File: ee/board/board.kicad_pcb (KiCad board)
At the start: 4 copper layers, 90 x 50 mm, 63 parts, among them J2 USB_A, J3 Micro_SD_Card_Det_Hirose_DM3AT, J4 Conn_01x08_Pin, J5 Conn_01x10_Pin, J6 Conn_Coaxial, SW1 SW_Push, U1 JW5211, U2 JW5211, U3 JW5211, U4 F1C100s, U5 SST26VF080A-104I/SN, U6 USBLC6-2SC6, U7 ATECC608A-SSHDA, Y1 Crystal_GND24

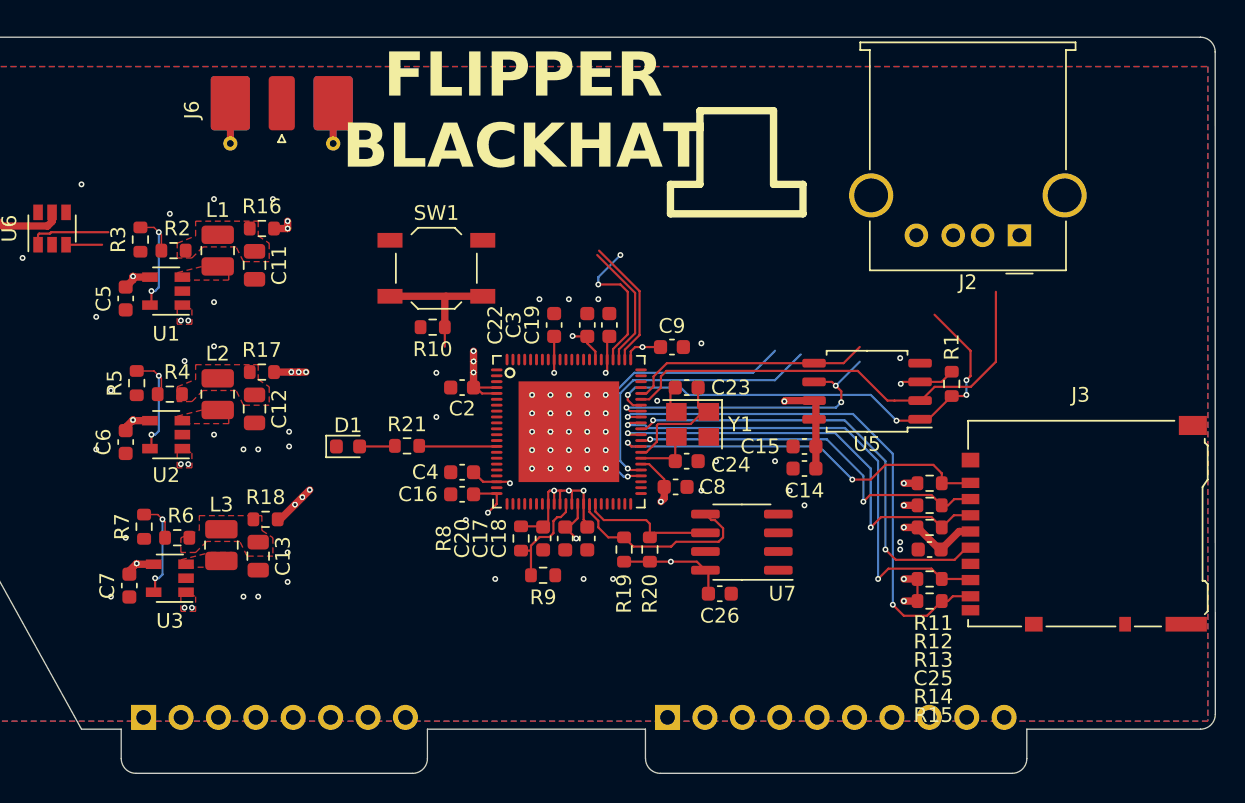
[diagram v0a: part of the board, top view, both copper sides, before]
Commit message: Dropped in the M.2 connectors.
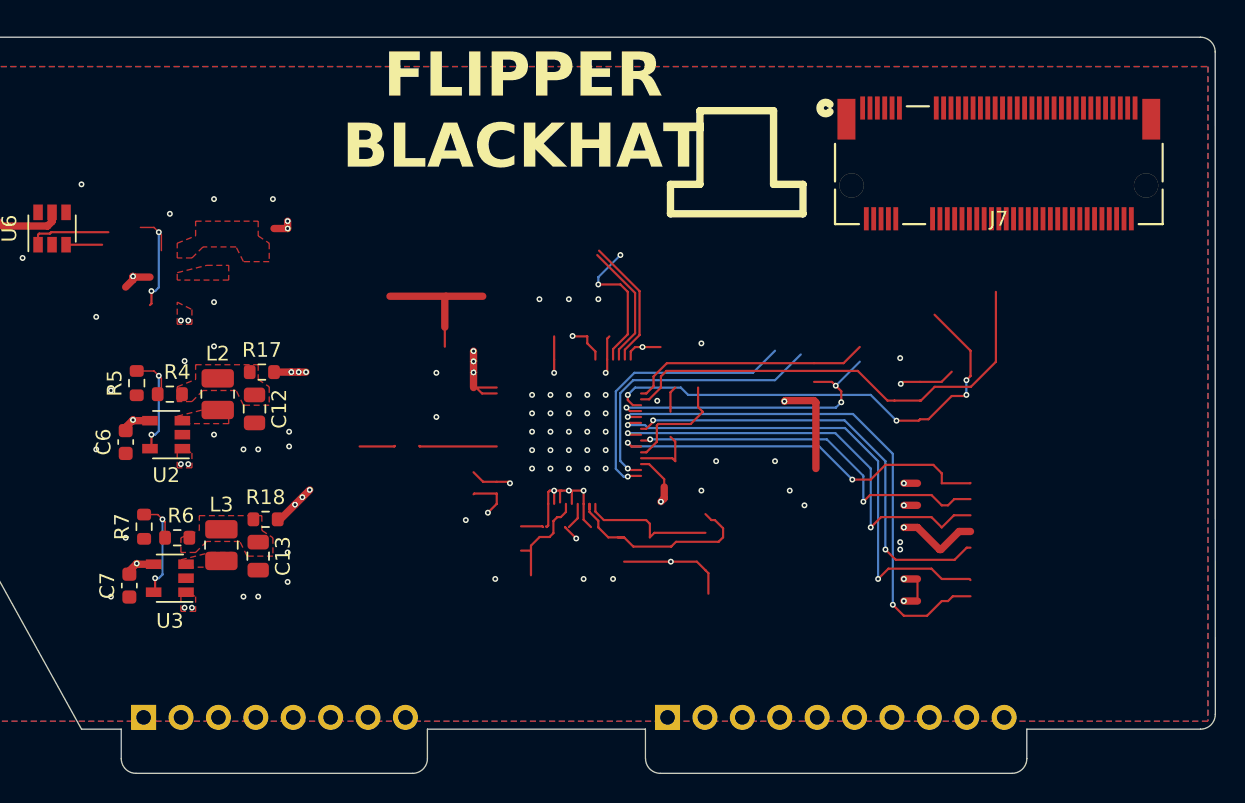
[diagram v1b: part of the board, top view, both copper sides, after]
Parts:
- removed C11: 22uF, Capacitor_SMD:C_0805_2012Metric
- removed C14, C15, C16, C2, C22, C25, C26, C3, C4, C8: 100nF, Capacitor_SMD:C_0603_1608Metric
- removed C17, C18, C19, C20, C5, C9: 2.2uF, Capacitor_SMD:C_0603_1608Metric
- removed C23, C24: 30pF, Capacitor_SMD:C_0603_1608Metric
- removed D1: LED, LED_SMD:LED_0603_1608Metric
- removed J2: USB_A, Connector_USB:USB_A_Molex_67643_Horizontal
- removed J3: Micro_SD_Card_Det_Hirose_DM3AT, Connector_Card:microSD_HC_Hirose_DM3AT-SF-PEJM5
- removed J6: Conn_Coaxial, Connector_Coaxial:SMA_Molex_73251-2120_EdgeMount_Horizontal
- removed L1: 1.5uH, Inductor_SMD:L_1008_2520Metric
- removed R1, R10: 10k, Resistor_SMD:R_0603_1608Metric
- removed R11, R12, R13, R14, R15: 47k, Resistor_SMD:R_0603_1608Metric
- removed R16: 0R, Resistor_SMD:R_0603_1608Metric
- removed R19, R20, R21: 4.7k, Resistor_SMD:R_0603_1608Metric
- removed R2: 49.9k, Resistor_SMD:R_0603_1608Metric
- removed R3: 11k, Resistor_SMD:R_0603_1608Metric
- removed R8, R9: 2.2k, Resistor_SMD:R_0603_1608Metric
- removed SW1: SW_Push, Button_Switch_SMD:SW_SPST_TL3342
- removed U1: JW5211, Package_TO_SOT_SMD:SOT-23-5
- removed U4: F1C100s, 3340:QFN-88_EP_10x10_Pitch0.4mm
- removed U5: SST26VF080A-104I/SN, Package_SO:SOIC-8_5.275x5.275mm_P1.27mm
- removed U7: ATECC608A-SSHDA, Package_SO:SOIC-8_3.9x4.9mm_P1.27mm
- removed Y1: Crystal_GND24, Crystal:Crystal_SMD_Abracon_ABM8G-4Pin_3.2x2.5mm
- added J7: Conn_01x20_Pin, 2199119-5:CONN75_2199119-5_TEC, F.Cu at (175.3, 98.7)
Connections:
- U6 pad 4: Net-(J2-D+) -> unconnected-(U6-I/O2-Pad4)
- U6 pad 6: Net-(J2-D-) -> unconnected-(U6-I/O1-Pad6)
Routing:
- net (no net): track 0.00 -> 402.4 mm, vias 0 -> 25
- net /SDC0_D1: track 36.5 -> 0.00 mm, vias 2 -> 0
- net /SDC0_D0: track 33.9 -> 0.00 mm, vias 2 -> 0
- net /SPI_CS: track 32.7 -> 0.00 mm, vias 4 -> 0
- net /SPI_MISO: track 32.0 -> 0.00 mm
- net /SDC0_CLK: track 30.5 -> 0.00 mm, vias 2 -> 0
- net /SDC0_CMD: track 30.1 -> 0.00 mm, vias 2 -> 0
- net /SDC0_D2: track 26.7 -> 0.00 mm, vias 2 -> 0
- net /SDC0_D3: track 25.8 -> 0.00 mm, vias 2 -> 0
- net /SPI_CK: track 21.0 -> 0.00 mm, vias 3 -> 0
- net /UART_RX: track 19.6 -> 0.00 mm, vias 1 -> 0
- net /!RST: track 19.6 -> 0.00 mm, vias 2 -> 0
- net /UART_TX: track 19.2 -> 0.00 mm, vias 1 -> 0
- net /SPI_MOSI: track 16.5 -> 0.00 mm
- net /TWI0_SDA: track 14.1 -> 0.00 mm
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- added copper zone on F.Cu, net (none)
- removed copper zone on F.Cu, net Net-(C11-Pad1)
- removed copper zone on F.Cu, net Net-(L1-Pad1)

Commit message: Added in module
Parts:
- removed C12, C13: 22uF, Capacitor_SMD:C_0805_2012Metric
- removed C6, C7: 2.2uF, Capacitor_SMD:C_0603_1608Metric
- removed F1: 330 mA, Fuse:Fuse_0603_1608Metric
- removed J7: Conn_01x20_Pin, 2199119-5:CONN75_2199119-5_TEC
- removed L2, L3: 1.5uH, Inductor_SMD:L_1008_2520Metric
- removed R17, R18: 0R, Resistor_SMD:R_0603_1608Metric
- removed R4: 36k, Resistor_SMD:R_0603_1608Metric
- removed R5: 11k, Resistor_SMD:R_0603_1608Metric
- removed R6: 8.2k, Resistor_SMD:R_0603_1608Metric
- removed R7: 10k, Resistor_SMD:R_0603_1608Metric
- removed U2, U3: JW5211, Package_TO_SOT_SMD:SOT-23-5
- added J1: Lichee_RV_J3, 2199119-5:CONN75_2199119-5_TEC, F.Cu at (164.0, 125.0)
- added J2: Lichee_RV_J4, 2199119-5:CONN75_2199119-5_TEC, F.Cu at (139.8, 125.0)
- added J3: USB_A, Connector_USB:USB_A_Receptacle_GCT_USB1046, F.Cu at (109.2, 99.1)
- added R1: 22R, Resistor_SMD:R_0603_1608Metric, F.Cu at (124.9, 104.2)
- added R2: 22R, Resistor_SMD:R_0603_1608Metric, F.Cu at (124.9, 106.7)
- moved U6 9.93 mm to (110.2, 112.9), turned to -90 degrees
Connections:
- J5 pad 5: /TX -> /UART_TXD
- J5 pad 6: /RX -> /UART_RXD
- U6 pad 1: /USB_N -> Net-(R2-Pad1)
- U6 pad 3: /USB_P -> Net-(R1-Pad1)
- U6 pad 4: unconnected-(U6-I/O2-Pad4) -> Net-(J3-D+)
- U6 pad 5: VBUS -> +5V
- U6 pad 6: unconnected-(U6-I/O1-Pad6) -> Net-(J3-D-)
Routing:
- net (no net): track 402.4 -> 0.00 mm, vias 25 -> 1
- net +3V3: track 47.9 -> 0.00 mm, vias 17 -> 0
- net +2V5: track 16.4 -> 0.00 mm, vias 9 -> 0
- net /USB_N: track 14.5 -> 0.00 mm
- net +1V1: track 11.6 -> 0.00 mm, vias 6 -> 0
- net /USB_P: track 11.1 -> 0.00 mm
- net VBUS: track 9.66 -> 0.00 mm
- net /2v5_FB: track 8.05 -> 0.00 mm, vias 2 -> 0
- net /1v1_FB: track 8.05 -> 0.00 mm, vias 2 -> 0
- net +5V: track 6.60 -> 0.00 mm, vias 19 -> 0
- net Net-(U2-EN): track 4.21 -> 0.00 mm, vias 2 -> 0
- net GND: track 1.78 -> 0.00 mm, vias 64 -> 0
- removed copper zone on F.Cu, net (none)
- removed copper zone on In1.Cu, net +1V1
- removed copper zone on In1.Cu, net +2V5
- removed copper zone on In1.Cu, net +3V3
- removed copper zone on F.Cu, net +5V
- removed copper zone on In1.Cu, net +5V
- removed copper zone on F.Cu, net Net-(C12-Pad1)
- removed copper zone on F.Cu, net Net-(C13-Pad1)
- removed copper zone on F.Cu, net Net-(U2-SW)
- removed copper zone on F.Cu, net Net-(U3-SW)

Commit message: Schematic mostly finished.
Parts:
- added C1: 10uF, Capacitor_SMD:C_0603_1608Metric, F.Cu at (139.7, 105.7)
- added C10: 100nF, Capacitor_SMD:C_0603_1608Metric, F.Cu at (217.9, 96.7)
- added C11: 100nF, Capacitor_SMD:C_0603_1608Metric, F.Cu at (217.9, 99.2)
- added C12: 100nF, Capacitor_SMD:C_0603_1608Metric, F.Cu at (217.9, 101.8)
- added C13: 22nF, Capacitor_SMD:C_0603_1608Metric, F.Cu at (176.3, 117.5)
- added C14: 18pF, Capacitor_SMD:C_0603_1608Metric, F.Cu at (221.9, 91.7)
- added C15: 18pF, Capacitor_SMD:C_0603_1608Metric, F.Cu at (221.9, 94.2)
- added C18: 22nF, Capacitor_SMD:C_0603_1608Metric, F.Cu at (221.9, 96.7)
- added C2: 10uF, Capacitor_SMD:C_0603_1608Metric, F.Cu at (139.7, 108.2)
- added C3: 10uF, Capacitor_SMD:C_0603_1608Metric, F.Cu at (139.7, 110.7)
- added C4: 10uF, Capacitor_SMD:C_0603_1608Metric, F.Cu at (139.7, 113.2)
- added C5: NC, Capacitor_SMD:C_0603_1608Metric, F.Cu at (139.7, 115.7)
- added C6: NC, Capacitor_SMD:C_0603_1608Metric, F.Cu at (151.4, 117.8)
- added C7: NC, Capacitor_SMD:C_0603_1608Metric, F.Cu at (151.4, 120.4)
- added C8: 100nF, Capacitor_SMD:C_0603_1608Metric, F.Cu at (217.9, 91.7)
- added C9: 1nF, Capacitor_SMD:C_0603_1608Metric, F.Cu at (217.9, 94.2)
- added H1: M2.5 Spacer, KiLib:9774025151R, F.Cu at (139.7, 105.7)
- added J6: Conn_Coaxial, Connector_Coaxial:SMA_Amphenol_901-143_Horizontal, F.Cu at (143.9, 96.5)
- added J8: HR911105A, KiLib:HR911105a, F.Cu at (171.0, 103.2)
- added JP1: SolderJumper_2_Bridged, Jumper:SolderJumper-2_P1.3mm_Bridged2Bar_RoundedPad1.0x1.5mm, F.Cu at (154.3, 104.2)
- added JP2: SolderJumper_2_Bridged, Jumper:SolderJumper-2_P1.3mm_Bridged2Bar_RoundedPad1.0x1.5mm, F.Cu at (155.6, 118.4)
- added JP3: SolderJumper_2_Bridged, Jumper:SolderJumper-2_P1.3mm_Bridged2Bar_RoundedPad1.0x1.5mm, F.Cu at (155.6, 121.9)
- added R13: 10k, Resistor_SMD:R_0603_1608Metric, F.Cu at (194.1, 74.8)
- added R14: 0R, Resistor_SMD:R_0603_1608Metric, F.Cu at (194.1, 77.9)
- added R15: 100K, Resistor_SMD:R_0603_1608Metric, F.Cu at (191.3, 64.7)
- added R16: 1k, Resistor_SMD:R_0603_1608Metric, F.Cu at (184.3, 64.7)
- added R17: 1k, Resistor_SMD:R_0603_1608Metric, F.Cu at (181.1, 64.7)
- added R18: 10K, Resistor_SMD:R_0603_1608Metric, F.Cu at (151.4, 112.2)
- added R19: 100R, Resistor_SMD:R_0603_1608Metric, F.Cu at (151.4, 122.9)
- added R21: 5.1k, Resistor_SMD:R_0603_1608Metric, F.Cu at (221.9, 99.2)
- added R3: 0R, Resistor_SMD:R_0603_1608Metric, F.Cu at (159.2, 96.5)
- added R30: 5.1k, Resistor_SMD:R_0603_1608Metric, F.Cu at (225.9, 104.3)
- added R31: 470R, Resistor_SMD:R_0603_1608Metric, F.Cu at (229.9, 91.7)
- added R32: 5.1k, Resistor_SMD:R_0603_1608Metric, F.Cu at (229.9, 94.2)
- added R33: 5.1k, Resistor_SMD:R_0603_1608Metric, F.Cu at (229.9, 96.7)
- added R34: 470R, Resistor_SMD:R_0603_1608Metric, F.Cu at (229.9, 99.2)
- added R4: 100K, Resistor_SMD:R_0603_1608Metric, F.Cu at (154.8, 96.5)
- added RN1: 10k, Resistor_SMD:R_Array_Convex_4x0402, F.Cu at (186.1, 80.6)
- added RN2: 10k, Resistor_SMD:R_Array_Convex_4x0402, F.Cu at (182.6, 80.6)
- added RN3: 10k, Resistor_SMD:R_Array_Convex_4x0402, F.Cu at (171.6, 124.0)
- added RN4: 10k, Resistor_SMD:R_Array_Convex_4x0402, F.Cu at (166.1, 118.2)
- added RN5: 22R, Resistor_SMD:R_Array_Convex_4x0402, F.Cu at (202.0, 110.3)
- added RN6: 22R, Resistor_SMD:R_Array_Convex_4x0402, F.Cu at (205.1, 110.3)
- added RN7: 22R, Resistor_SMD:R_Array_Convex_4x0402, F.Cu at (208.1, 110.3)
- added U1: RTL8201F, Package_DFN_QFN:QFN-32-1EP_5x5mm_P0.5mm_EP3.3x3.3mm, F.Cu at (170.6, 119.2)
- added U2: RTL8723DS, KiLib:RTL8723, F.Cu at (185.1, 72.8)
- added Y1: Crystal_GND24_Small, Crystal:Crystal_SMD_3225-4Pin_3.2x2.5mm, F.Cu at (225.8, 107.8)
- J1, J2: footprint 2199119-5:CONN75_2199119-5_TEC -> 2199119-5:CONN75_2199230-3
- moved J3 13.9 mm to (123.0, 97.5)
- moved U6 13.7 mm to (123.3, 109.0), turned to 90 degrees
- moved J2 13.2 mm to (127.6, 130.1)
- moved J1 13.2 mm to (151.8, 130.1)
- moved R1 9.19 mm to (122.3, 113.0), turned to -90 degrees
- moved R2 6.34 mm to (124.3, 113.0), turned to -90 degrees
- moved J4 3.20 mm to (118.3, 139.2)
- moved J5 3.20 mm to (153.9, 139.2)
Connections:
- J1 pad 1: /UART_RXD -> Net-(J1-PB8)
- J1 pad 3: /UART_TXD -> Net-(J1-PB9)
- J1 pad 39: unconnected-(J1-PE0-Pad39) -> Net-(J1-PE0)
- J1 pad 41: unconnected-(J1-PE2-Pad41) -> Net-(J1-PE2)
- J1 pad 43: unconnected-(J1-PE1-Pad43) -> Net-(J1-PE1)
- J1 pad 45: unconnected-(J1-PE3-Pad45) -> /RMII_TXCK
- J1 pad 47: unconnected-(J1-PE4-Pad47) -> Net-(J1-PE4)
- J1 pad 49: unconnected-(J1-PE5-Pad49) -> Net-(J1-PE5)
- J1 pad 51: unconnected-(J1-PE7-Pad51) -> Net-(J1-PE7)
- J1 pad 53: unconnected-(J1-PE6-Pad53) -> Net-(J1-PE6)
- J1 pad 55: unconnected-(J1-PE8-Pad55) -> Net-(J1-PE8)
- J1 pad 57: unconnected-(J1-PE9-Pad57) -> Net-(J1-PE9)
- J1 pad 71: unconnected-(J1-PE16-Pad71) -> Net-(J1-PE16)
- J2 pad 10: unconnected-(J2-SYS_RST-Pad10) -> Net-(J2-SYS_RST)
- J2 pad 20: unconnected-(J2-PG8-Pad20) -> /PG8_AP_UART1_RTS
- J2 pad 22: unconnected-(J2-MIPI_DSI_D3_N-Pad22) -> /PG9_AP_UART1_CTS
- J2 pad 23: unconnected-(J2-PG7-Pad23) -> /PG7_AP_UART1_RX
- J2 pad 24: unconnected-(J2-MIPI_DSI_D3_P-Pad24) -> /PG10_WL_WAKE_AP
- J2 pad 25: unconnected-(J2-PG3-Pad25) -> /PG3_SDIO1_D1
- J2 pad 26: GND -> /PG11_CLK_FANOUT
- J2 pad 27: unconnected-(J2-PG4-Pad27) -> /PG4_SDIO1_D2
- J2 pad 28: unconnected-(J2-MIPI_DSI_D2_N-Pad28) -> /PG12_WL_REG_ON
- J2 pad 29: unconnected-(J2-PG2-Pad29) -> /PG2_SDIO1_D0
- J2 pad 31: unconnected-(J2-PG1-Pad31) -> /PG1_SDIO1_CMD
- J2 pad 32: GND -> unconnected-(J2-PG14-Pad32)
- J2 pad 33: unconnected-(J2-PG0-Pad33) -> /PG0_SDIO1_CLK
- J2 pad 35: unconnected-(J2-PG5-Pad35) -> /PG5_SDIO1_D3
- J2 pad 36: unconnected-(J2-MIPI_DSI_CK_P-Pad36) -> /PG17_BT_WAKE_AP
- J2 pad 37: unconnected-(J2-PG6-Pad37) -> /PG6_AP_UART1_TX
- J2 pad 38: GND -> /PG18_BT_RESETN
- J2 pad 40: unconnected-(J2-MIPI_DSI_D1_N-Pad40) -> /PG16_AP_WAKE_BT
- J2 pad 44: GND -> unconnected-(J2-ADC_GPADC1-Pad44)
- J2 pad 50: GND -> unconnected-(J2-AUDIO_HP_OUTFB-Pad50)
- J2 pad 56: unconnected-(J2-PD16-Pad56) -> GND
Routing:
- net (no net): vias 1 -> 0
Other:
- board size 90 x 50 mm -> 87.1 x 51 mm

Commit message: Moved some of the local library stuff into the submodule.
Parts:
- J1, J2: footprint 2199119-5:CONN75_2199230-3 -> KiLib:CONN75_2199230-3
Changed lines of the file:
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@@
     )
   )
-  (footprint "2199119-5:CONN75_2199230-3" (layer "F.Cu")
+  (footprint "KiLib:CONN75_2199230-3" (layer "F.Cu")
     (at 127.612499 130.1 180)
     (tags "2199119-5 ")
@@
     (pad "78" thru_hole circle (at -10 1.3765 270) (size 1 1) (drill 1) (layers "*.Cu" "*.Mask"))
     (pad "79" thru_hole circle (at 10 1.3765 270) (size 1.651 1.651) (drill 1.651) (layers "*.Cu" "*.Mask"))
-    (model "../2199230-3.step"
+    (model "step/2199230-3.step"
       (offset (xyz 0 -3.8 2.4))
       (scale (xyz 1 1.1 1))
@@
     )
   )
-  (footprint "2199119-5:CONN75_2199230-3" (layer "F.Cu")
+  (footprint "KiLib:CONN75_2199230-3" (layer "F.Cu")
     (at 151.772499 130.1 180)
     (tags "2199119-5 ")
@@
     (pad "78" thru_hole circle (at -10 1.3765 270) (size 1 1) (drill 1) (layers "*.Cu" "*.Mask"))
     (pad "79" thru_hole circle (at 10 1.3765 270) (size 1.651 1.651) (drill 1.651) (layers "*.Cu" "*.Mask"))
-    (model "../2199230-3.step"
+    (model "step/2199230-3.step"
       (offset (xyz 0 -3.8 2.4))
       (scale (xyz 1 1.1 1))
       (rotate (xyz -90 0 0))
     )
-    (model "../Lichee_RV_7001_3D.step"
-      (offset (xyz 35.15 0.8 3.6))
-      (scale (xyz 1 1 1))
-      (rotate (xyz 0 0 180))
-    )
-  )
+  )
